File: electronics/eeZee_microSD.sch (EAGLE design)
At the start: 12 parts, among them U1 MIC5317, U2 74HC4050, U4 MICROSD_CD

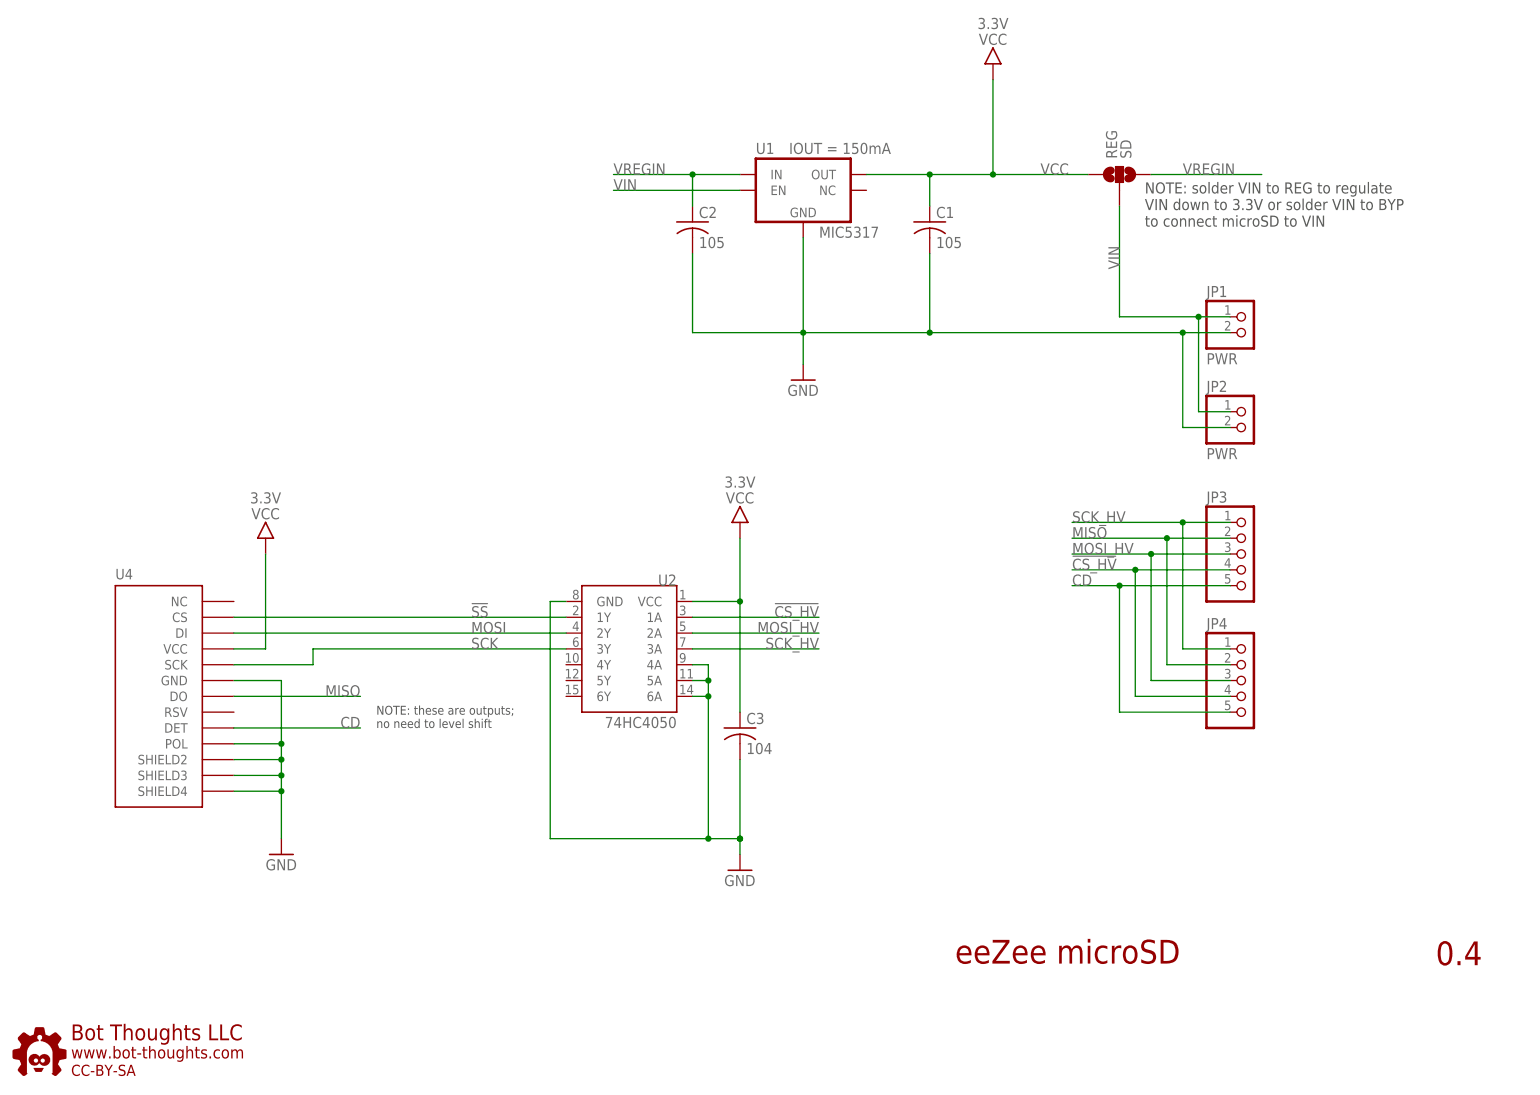
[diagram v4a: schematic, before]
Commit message: changed layout, silk, reg/byp, pwr routing, sd package (centered)
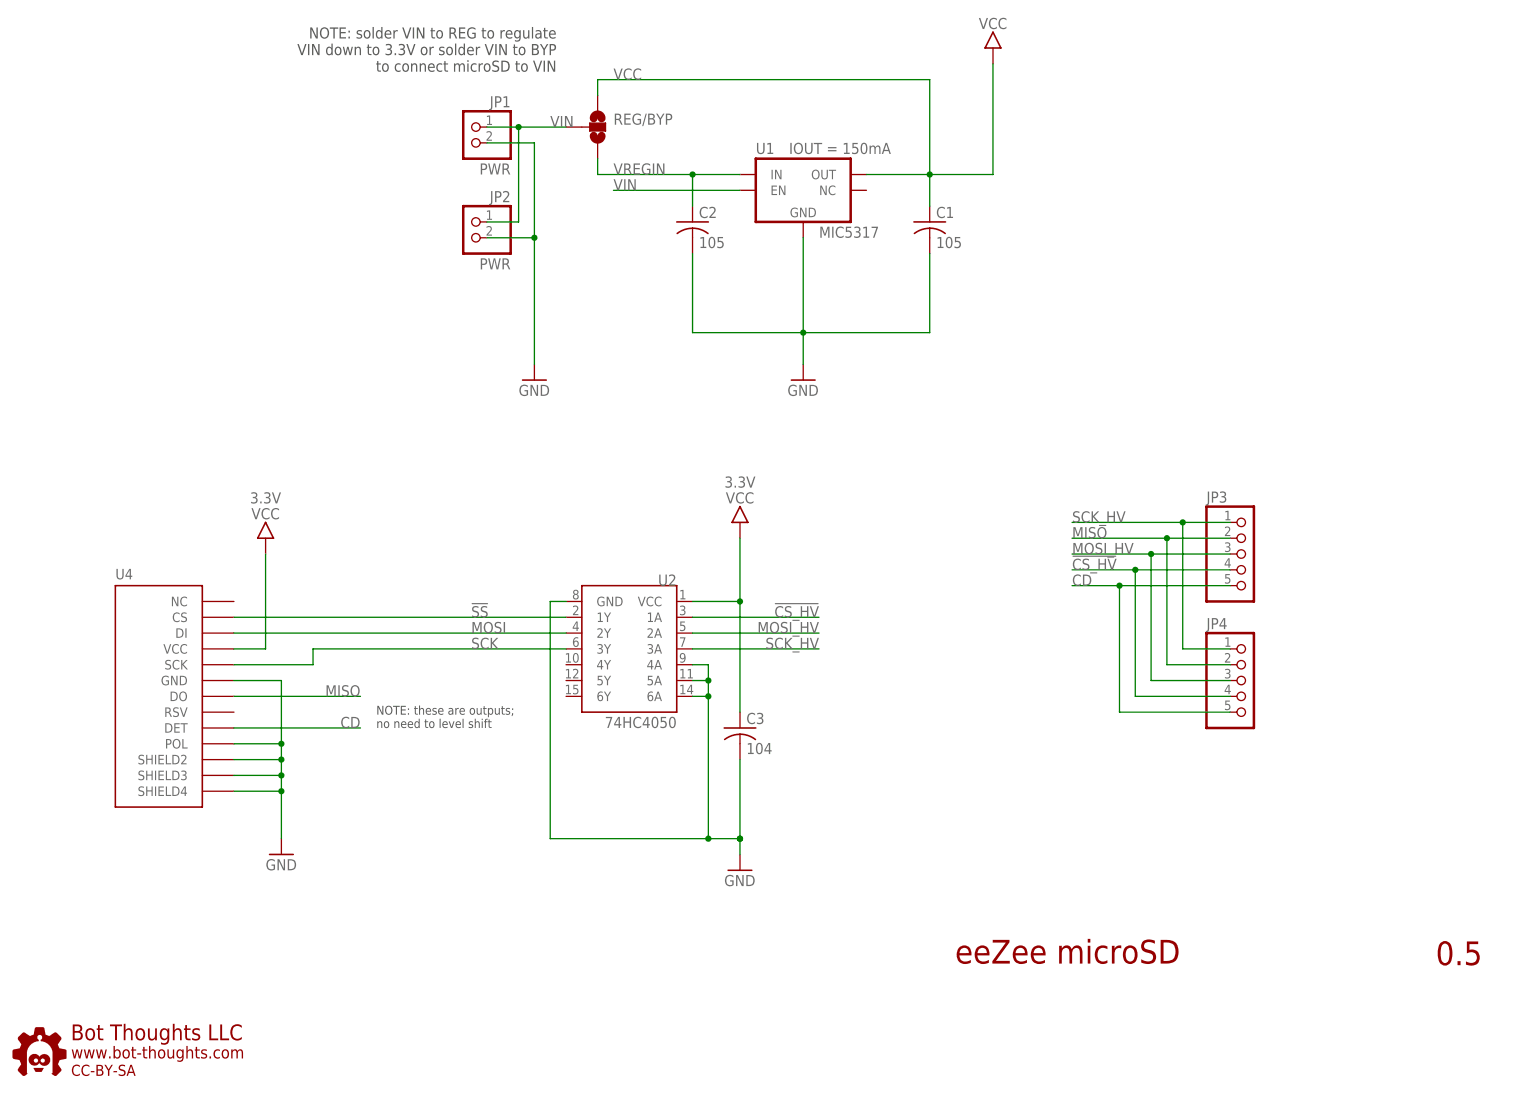
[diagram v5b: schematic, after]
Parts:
- removed REG: SD, SparkFun:SOLDERJUMPER_2WAYS
- added REG/BYP: (no value), SparkFun:SOLDERJUMPER_2WAYS
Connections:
- net VCC: now also REG/BYP.1; no longer REG.1
- net VIN: now also REG/BYP.2; no longer REG.2
- net VREGIN: now also REG/BYP.3; no longer REG.3
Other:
- note added: "0.5"
- note removed: "0.4"
- moved on the sheet: JP1, JP2
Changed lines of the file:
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@@
 <attribute name="PARTNO" value="LMK107B7105KA-T"/>
 </part>
-<part name="REG" library="SparkFun" deviceset="SOLDERJUMPER_2WAY" device="S" value="SD"/>
+<part name="REG/BYP" library="SparkFun" deviceset="SOLDERJUMPER_2WAY" device="S"/>
 <part name="FRAME1" library="mes" deviceset="LETTER_L" device=""/>
 <part name="GND2" library="mes" deviceset="GND" device=""/>
@@
 </part>
 <part name="GND5" library="mes" deviceset="GND" device=""/>
-<part name="U$2" library="bt" deviceset="VCC" device="" value="3.3V"/>
+<part name="U$2" library="bt" deviceset="VCC" device=""/>
 <part name="U$3" library="bt" deviceset="VCC" device="" value="3.3V"/>
 <part name="U$4" library="bt" deviceset="VCC" device="" value="3.3V"/>
@@
 <attribute name="PARTNO" value="LMK107B7105KA-T"/>
 </part>
+<part name="GND3" library="mes" deviceset="GND" device=""/>
 </parts>
 <sheets>
 <sheet>
 <plain>
-<text x="184.404" y="148.59" size="1.778" layer="97" align="top-left">NOTE: solder VIN to REG to regulate
+<text x="89.916" y="166.37" size="1.778" layer="97" rot="R180" align="top-left">NOTE: solder VIN to REG to regulate
 VIN down to 3.3V or solder VIN to BYP
 to connect microSD to VIN</text>
 <text x="153.924" y="23.114" size="3.81" layer="94">eeZee microSD</text>
-<text x="231.14" y="22.86" size="3.81" layer="94">0.4</text>
+<text x="231.14" y="22.86" size="3.81" layer="94">0.5</text>
 <text x="60.96" y="60.96" size="1.4224" layer="97">NOTE: these are outputs;
 no need to level shift</text>
 </plain>
 <instances>
-<instance part="JP1" gate="A" x="200.66" y="124.46"/>
+<instance part="JP1" gate="A" x="76.2" y="154.94" rot="MR0"/>
 <instance part="U1" gate="U1" x="129.54" y="147.32">
 <attribute name="PARTNO" value="MIC5205-3.3YM5 TR" x="129.54" y="147.32" size="1.778" layer="96" display="off"/>
@@
 <attribute name="PARTNO" value="JMK212BJ226MG-T" x="149.86" y="142.24" size="1.778" layer="96" display="off"/>
 </instance>
-<instance part="REG" gate="G$1" x="180.34" y="149.86" rot="R90"/>
+<instance part="REG/BYP" gate="G$1" x="96.52" y="157.48"/>
 <instance part="FRAME1" gate="G$1" x="0" y="0"/>
 <instance part="FRAME1" gate="G$2" x="147.32" y="2.54"/>
@@
 </instance>
 <instance part="GND5" gate="1" x="119.38" y="38.1"/>
-<instance part="U$2" gate="G$1" x="160.02" y="165.1"/>
+<instance part="U$2" gate="G$1" x="160.02" y="167.64"/>
 <instance part="U$3" gate="G$1" x="119.38" y="91.44"/>
 <instance part="U$4" gate="G$1" x="43.18" y="88.9"/>
-<instance part="JP2" gate="A" x="200.66" y="109.22"/>
+<instance part="JP2" gate="A" x="76.2" y="139.7" rot="MR0"/>
 <instance part="GND1" gate="1" x="45.72" y="40.64"/>
 <instance part="JP4" gate="A" x="200.66" y="68.58"/>
@@
 <attribute name="PARTNO" value="JMK212BJ226MG-T" x="111.76" y="142.24" size="1.778" layer="96" display="off"/>
 </instance>
+<instance part="GND3" gate="1" x="86.36" y="116.84"/>
 </instances>
 <busses>
@@
 </segment>
 <segment>
+<pinref part="JP1" gate="A" pin="2"/>
+<wire x1="78.74" y1="154.94" x2="86.36" y2="154.94" width="0.1524" layer="91"/>
+<pinref part="JP2" gate="A" pin="2"/>
+<wire x1="78.74" y1="139.7" x2="86.36" y2="139.7" width="0.1524" layer="91"/>
+<wire x1="86.36" y1="139.7" x2="86.36" y2="154.94" width="0.1524" layer="91"/>
+<junction x="86.36" y="139.7"/>
+<wire x1="86.36" y1="139.7" x2="86.36" y2="119.38" width="0.1524" layer="91"/>
+<pinref part="GND3" gate="1" pin="GND"/>
+</segment>
+<segment>
 <wire x1="149.86" y1="124.46" x2="129.54" y2="124.46" width="0.1524" layer="91"/>
 <pinref part="U1" gate="U1" pin="GND"/>
@@
 <pinref part="C1" gate="C1" pin="-"/>
 <wire x1="149.86" y1="137.16" x2="149.86" y2="124.46" width="0.1524" layer="91"/>
-<junction x="149.86" y="124.46"/>
 <pinref part="GND2" gate="1" pin="GND"/>
 <wire x1="129.54" y1="119.38" x2="129.54" y2="124.46" width="0.1524" layer="91"/>
-<pinref part="JP1" gate="A" pin="2"/>
-<wire x1="198.12" y1="124.46" x2="190.5" y2="124.46" width="0.1524" layer="91"/>
-<pinref part="JP2" gate="A" pin="2"/>
-<wire x1="190.5" y1="124.46" x2="149.86" y2="124.46" width="0.1524" layer="91"/>
-<wire x1="198.12" y1="109.22" x2="190.5" y2="109.22" width="0.1524" layer="91"/>
-<wire x1="190.5" y1="109.22" x2="190.5" y2="124.46" width="0.1524" layer="91"/>
-<junction x="190.5" y="124.46"/>
 <pinref part="C2" gate="C1" pin="-"/>
 <wire x1="129.54" y1="124.46" x2="111.76" y2="124.46" width="0.1524" layer="91"/>
@@
 <net name="VREGIN" class="0">
 <segment>
-<pinref part="REG" gate="G$1" pin="3"/>
-<wire x1="203.2" y1="149.86" x2="185.42" y2="149.86" width="0.1524" layer="91"/>
-<label x="190.5" y="149.86" size="1.778" layer="95"/>
-</segment>
-<segment>
 <pinref part="U1" gate="U1" pin="IN"/>
-<wire x1="99.06" y1="149.86" x2="111.76" y2="149.86" width="0.1524" layer="91"/>
 <label x="99.06" y="149.86" size="1.778" layer="95"/>
 <pinref part="C2" gate="C1" pin="+"/>
@@
 <wire x1="111.76" y1="144.78" x2="111.76" y2="149.86" width="0.1524" layer="91"/>
 <junction x="111.76" y="149.86"/>
+<pinref part="REG/BYP" gate="G$1" pin="3"/>
+<wire x1="111.76" y1="149.86" x2="96.52" y2="149.86" width="0.1524" layer="91"/>
+<wire x1="96.52" y1="149.86" x2="96.52" y2="152.4" width="0.1524" layer="91"/>
 </segment>
 </net>
 <net name="VIN" class="0">
 <segment>
-<pinref part="REG" gate="G$1" pin="2"/>
-<wire x1="180.34" y1="144.78" x2="180.34" y2="127" width="0.1524" layer="91"/>
+<pinref part="REG/BYP" gate="G$1" pin="2"/>
 <pinref part="JP1" gate="A" pin="1"/>
-<wire x1="198.12" y1="127" x2="193.04" y2="127" width="0.1524" layer="91"/>
-<label x="180.34" y="134.62" size="1.778" layer="95" rot="R90"/>
+<wire x1="78.74" y1="157.48" x2="83.82" y2="157.48" width="0.1524" layer="91"/>
 <pinref part="JP2" gate="A" pin="1"/>
-<wire x1="193.04" y1="127" x2="180.34" y2="127" width="0.1524" layer="91"/>
-<wire x1="198.12" y1="111.76" x2="193.04" y2="111.76" width="0.1524" layer="91"/>
-<wire x1="193.04" y1="111.76" x2="193.04" y2="127" width="0.1524" layer="91"/>
-<junction x="193.04" y="127"/>
+<wire x1="83.82" y1="157.48" x2="91.44" y2="157.48" width="0.1524" layer="91"/>
+<wire x1="78.74" y1="142.24" x2="83.82" y2="142.24" width="0.1524" layer="91"/>
+<wire x1="83.82" y1="142.24" x2="83.82" y2="157.48" width="0.1524" layer="91"/>
+<junction x="83.82" y="157.48"/>
+<label x="88.9" y="157.48" size="1.778" layer="95"/>
 </segment>
 <segment>
@@
 <net name="VCC" class="0">
 <segment>
+<pinref part="REG/BYP" gate="G$1" pin="1"/>
 <pinref part="U1" gate="U1" pin="OUT"/>
+<wire x1="96.52" y1="165.1" x2="96.52" y2="162.56" width="0.1524" layer="91"/>
 <wire x1="139.7" y1="149.86" x2="149.86" y2="149.86" width="0.1524" layer="91"/>
 <wire x1="149.86" y1="144.78" x2="149.86" y2="149.86" width="0.1524" layer="91"/>
 <pinref part="C1" gate="C1" pin="+"/>
 <junction x="149.86" y="149.86"/>
-<pinref part="REG" gate="G$1" pin="1"/>
 <wire x1="149.86" y1="149.86" x2="160.02" y2="149.86" width="0.1524" layer="91"/>
-<label x="167.64" y="149.86" size="1.778" layer="95"/>
-<wire x1="160.02" y1="149.86" x2="175.26" y2="149.86" width="0.1524" layer="91"/>
-<junction x="160.02" y="149.86"/>
 <pinref part="U$2" gate="G$1" pin="VCC"/>
-<wire x1="160.02" y1="149.86" x2="160.02" y2="165.1" width="0.1524" layer="91"/>
-</segment>
-<segment>
+<wire x1="160.02" y1="149.86" x2="160.02" y2="167.64" width="0.1524" layer="91"/>
+<wire x1="96.52" y1="165.1" x2="149.86" y2="165.1" width="0.1524" layer="91"/>
+<wire x1="149.86" y1="165.1" x2="149.86" y2="149.86" width="0.1524" layer="91"/>
+<label x="99.06" y="165.1" size="1.778" layer="95"/>
+</segment>
+<segment>
